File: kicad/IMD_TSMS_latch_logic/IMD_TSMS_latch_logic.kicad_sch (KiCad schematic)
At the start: 81 parts, among them IC1 NE555, J1 Conn_01x02, J3 Conn_01x02, J4 Conn_01x02, J5 Conn_01x02, J6 Conn_01x02, J7 Conn_01x02, J8 Conn_01x02, J9 Conn_01x02, K1 SANYOU_SRD_Form_C, K2 SANYOU_SRD_Form_C, Q2 AO3400A, Q3 AO3401A, Q5 AO3401A, Q6 AO3401A, SW1 SW_Push, U1 4001, U2 4009, U3 4009, U4 4001, U5 LTV-817S, U6 LM311

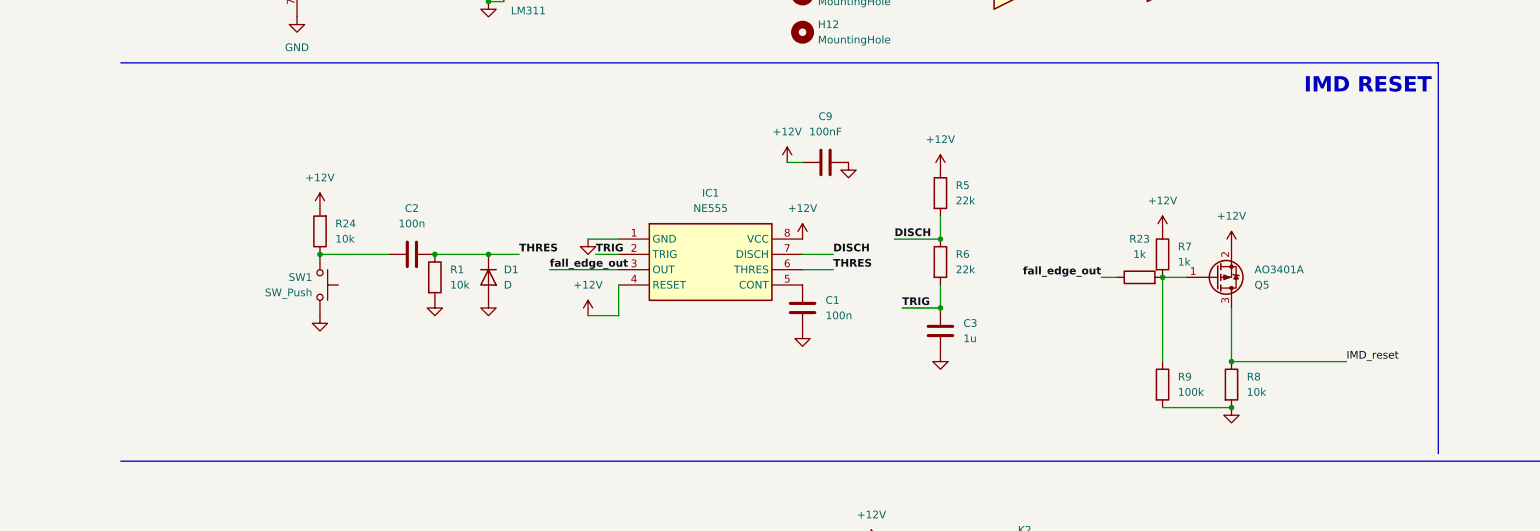
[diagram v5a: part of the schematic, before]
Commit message: update IMD reset
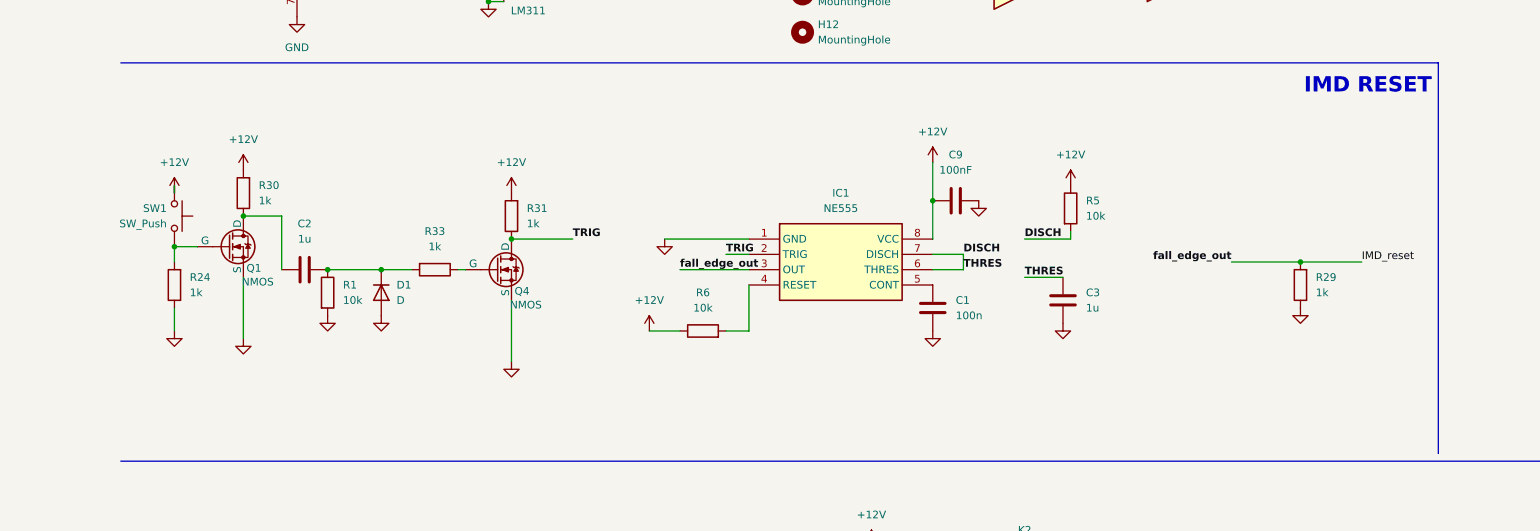
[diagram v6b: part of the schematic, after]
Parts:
- removed Q5: AO3401A, RMC_SOT:SOT-23, symbol Transistor_FET:AO3401A
- removed R23, R7: 1k, RMC_Resistor:R_0805_2012Metric_Pad1.20x1.40mm_HandSolder_L, symbol Device:R
- removed R8: 10k, RMC_Resistor:R_0805_2012Metric_Pad1.20x1.40mm_HandSolder_L, symbol Device:R
- removed R9: 100k, RMC_Resistor:R_0805_2012Metric_Pad1.20x1.40mm_HandSolder_L, symbol Device:R
- added Q1, Q4: NMOS, symbol Simulation_SPICE:NMOS
- added R29, R30, R31, R33: 1k, RMC_Resistor:R_0805_2012Metric_Pad1.20x1.40mm_HandSolder_L, symbol Device:R
- C2: value 100n -> 1u
- R24: value 10k -> 1k
- R5, R6: value 22k -> 10k
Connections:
- net fall_edge_out is gone; now on net IMD_reset: IC1.3 (OUT)
- net +12V: now also R6.1, SW1.2, R30.2, R31.2; no longer IC1.4 (RESET), R24.2
- net DISCH: now also C3.1, IC1.6 (THRES); no longer R6.1
- net GND: now also R24.1, Q1.3 (S), Q4.3 (S), R29.1; no longer SW1.1
- net IMD_reset: now also R29.2
- net TRIG: now also Q4.1 (D), R31.1; no longer C3.1, R6.2
- net THRES: no longer names the net of C2.2, D1.1 (K), R1.1
- net THRES: now also R33.2; no longer IC1.6 (THRES)
- new net: IC1.4 (RESET), R6.2
- new net: Q1.2 (G), R24.2, SW1.1
- new net: Q4.2 (G), R33.1
- new net: C2.1, Q1.1 (D), R30.1
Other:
- moved on the sheet: C1, C2, C3, C9, D1, IC1, R1, R24, R5, SW1

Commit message: pcb layout update
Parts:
- removed D1: D, Diode_SMD:D_SMA_Handsoldering, symbol Device:D
- added D1: SS34, extra_footprints:SS34 (1N5822), symbol extra_symbols:SS34
- C1, C10, C2, C3, C4, C5, C6, C7, C9: footprint RMC_Capacitor:C_0805_2012Metric_Pad1.18x1.45mm_HandSolder_L -> Capacitor_SMD:C_0805_2012Metric_Pad1.18x1.45mm_HandSolder
- C8: footprint RMC_Capacitor:CP_Radial_D6.3mm_P2.50mm_extended -> Capacitor_THT:CP_Radial_D6.3mm_P2.50mm
- D2, D3, D4, D5, D6, D7: footprint RMC_LED:LED_0805_2012Metric_Pad1.45x1.40mm_HandSolder -> LED_SMD:LED_0805_2012Metric_Pad1.15x1.40mm_HandSolder
- IC1, U6: footprint RMC_SO:SOIC-8_3.9x4.9mm_P1.27mm_RMC_Handsolder -> Package_SO:SOIC-8_3.9x4.9mm_P1.27mm
- Q1, Q4: footprint (none) -> Package_TO_SOT_SMD:SOT-23
- Q2, Q3, Q6: footprint RMC_SOT:SOT-23 -> Package_TO_SOT_SMD:SOT-23
- R1, R10, R11, R12, R13, R14, R15, R16, R17, R18, R19, R2, R20, R21, R22, R24, R25, R26, R27, R28, R29, R3, R30, R31, R32, R33, R35, R4, R5, R6: footprint RMC_Resistor:R_0805_2012Metric_Pad1.20x1.40mm_HandSolder_L -> Resistor_SMD:R_0805_2012Metric_Pad1.20x1.40mm_HandSolder
- U1, U4: footprint RMC_SO:SOIC127P600X175-14N -> RMC-KiCad:SOIC127P600X175-14N
- U2, U3: footprint RMC_SO:SOIC-16_3.9x9.9mm_P1.27mm_Handsolder -> Package_SO:SOIC-16_3.9x9.9mm_P1.27mm
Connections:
- net GND: now also D1.A
- net at C2.2, R1.1, R33.2: now also D1.C
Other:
- moved on the sheet: C2, Q1, Q4, R1, R24, R30, R31, R33, SW1
